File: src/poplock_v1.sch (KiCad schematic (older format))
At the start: 0 parts

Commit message: cicuito mic sem hierarquia
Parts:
- added C1: 10u, symbol C
- added Q?: MMBF170, SOT-23, symbol MMBF170
- added R1: 10000, symbol R
- added U?: MIC_ELECTRET, symbol MIC_ELECTRET
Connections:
- net labels added: +12V, GND, Output
- wire segments 0 -> 9
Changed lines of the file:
@@
 LIBS:valves
 LIBS:L293D
+LIBS:microphone
 LIBS:poplock_v1-cache
 EELAYER 25 0
@@
 F6 "DIRECTION_L" I L 8350 3550 60
 $EndSheet
+$Comp
+L MIC_ELECTRET U?
+U 1 1 57CDCC00
+P 4900 4350
+F 0 "U?" H 4900 4600 60  0000 C CNN
+F 1 "MIC_ELECTRET" H 4900 4000 60  0000 C CNN
+F 2 "" H 4900 4350 60  0000 C CNN
+F 3 "" H 4900 4350 60  0000 C CNN
+	1    4900 4350
+	1    0    0    -1
+$EndComp
+$Comp
+L MMBF170 Q?
+U 1 1 57CDE9F6
+P 5750 4050
+F 0 "Q?" H 5950 4125 50  0000 L CNN
+F 1 "MMBF170" H 5950 4050 50  0000 L CNN
+F 2 "SOT-23" H 5950 3975 50  0000 L CIN
+F 3 "" H 5750 4050 50  0000 L CNN
+	1    5750 4050
+	1    0    0    -1
+$EndComp
+Wire Wire Line
+	5200 4250 5550 4250
+Wire Wire Line
+	5550 4250 5550 4100
+$Comp
+L GND #PWR?
+U 1 1 57CDED40
+P 5950 4750
+F 0 "#PWR?" H 5950 4500 50  0001 C CNN
+F 1 "GND" H 5950 4600 50  0000 C CNN
+F 2 "" H 5950 4750 50  0000 C CNN
+F 3 "" H 5950 4750 50  0000 C CNN
+	1    5950 4750
+	1    0    0    -1
+$EndComp
+Wire Wire Line
+	5950 4450 5950 4750
+Wire Wire Line
+	5200 4450 5950 4450
+Wire Wire Line
+	5850 4250 5850 4450
+$Comp
+L R R1
+U 1 1 57CDF14B
+P 5850 3550
+F 0 "R1" V 5930 3550 50  0000 C CNN
+F 1 "10000" V 5850 3550 50  0000 C CNN
+F 2 "" V 5780 3550 50  0000 C CNN
+F 3 "" H 5850 3550 50  0000 C CNN
+	1    5850 3550
+	1    0    0    -1
+$EndComp
+Wire Wire Line
+	5850 3850 5850 3700
+Wire Wire Line
+	5850 3400 5850 3200
+$Comp
+L +12V #PWR?
+U 1 1 57CDFF14
+P 5850 3200
+F 0 "#PWR?" H 5850 3050 50  0001 C CNN
+F 1 "+12V" H 5850 3340 50  0000 C CNN
+F 2 "" H 5850 3200 50  0000 C CNN
+F 3 "" H 5850 3200 50  0000 C CNN
+	1    5850 3200
+	1    0    0    -1
+$EndComp
+$Comp
+L C C1
+U 1 1 57CE02A0
+P 6200 3800
+F 0 "C1" H 6225 3900 50  0000 L CNN
+F 1 "10u" H 6225 3700 50  0000 L CNN
+F 2 "" H 6238 3650 50  0000 C CNN
+F 3 "" H 6200 3800 50  0000 C CNN
+	1    6200 3800
+	0    1    1    0
+$EndComp
+Wire Wire Line
+	6050 3800 5850 3800
+Connection ~ 5850 3800
+Text GLabel 6550 3800 2    60   Input ~ 0
+Output
+Wire Wire Line
+	6350 3800 6550 3800
 $EndSCHEMATC

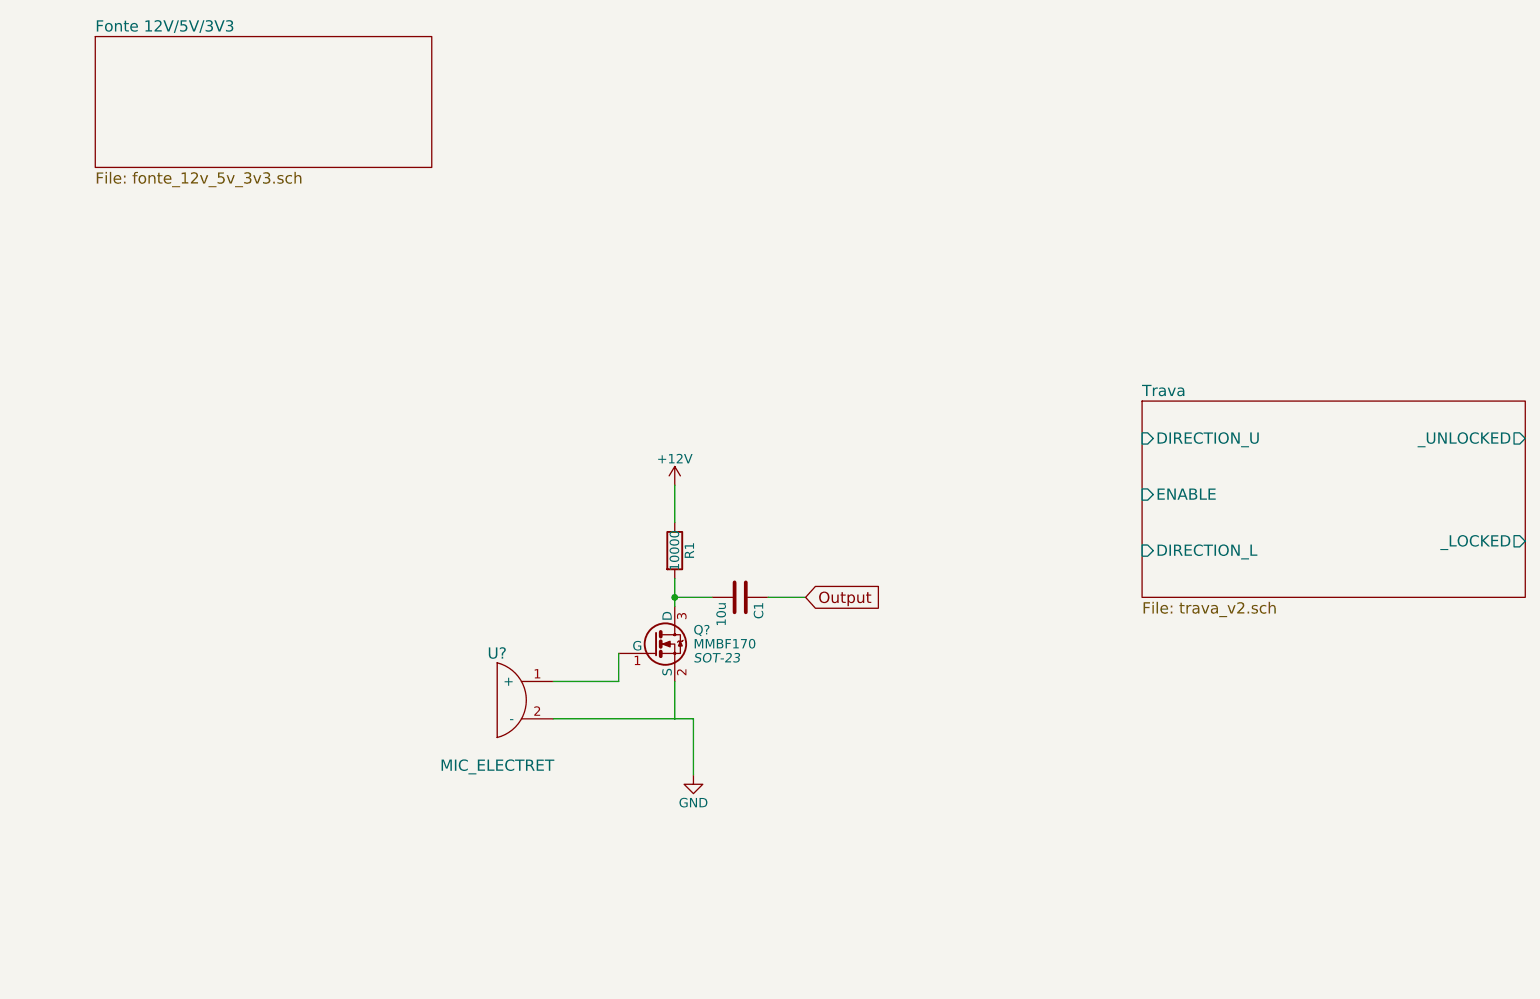
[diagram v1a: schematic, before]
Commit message: Criada hierarquia para o circuito do microfone
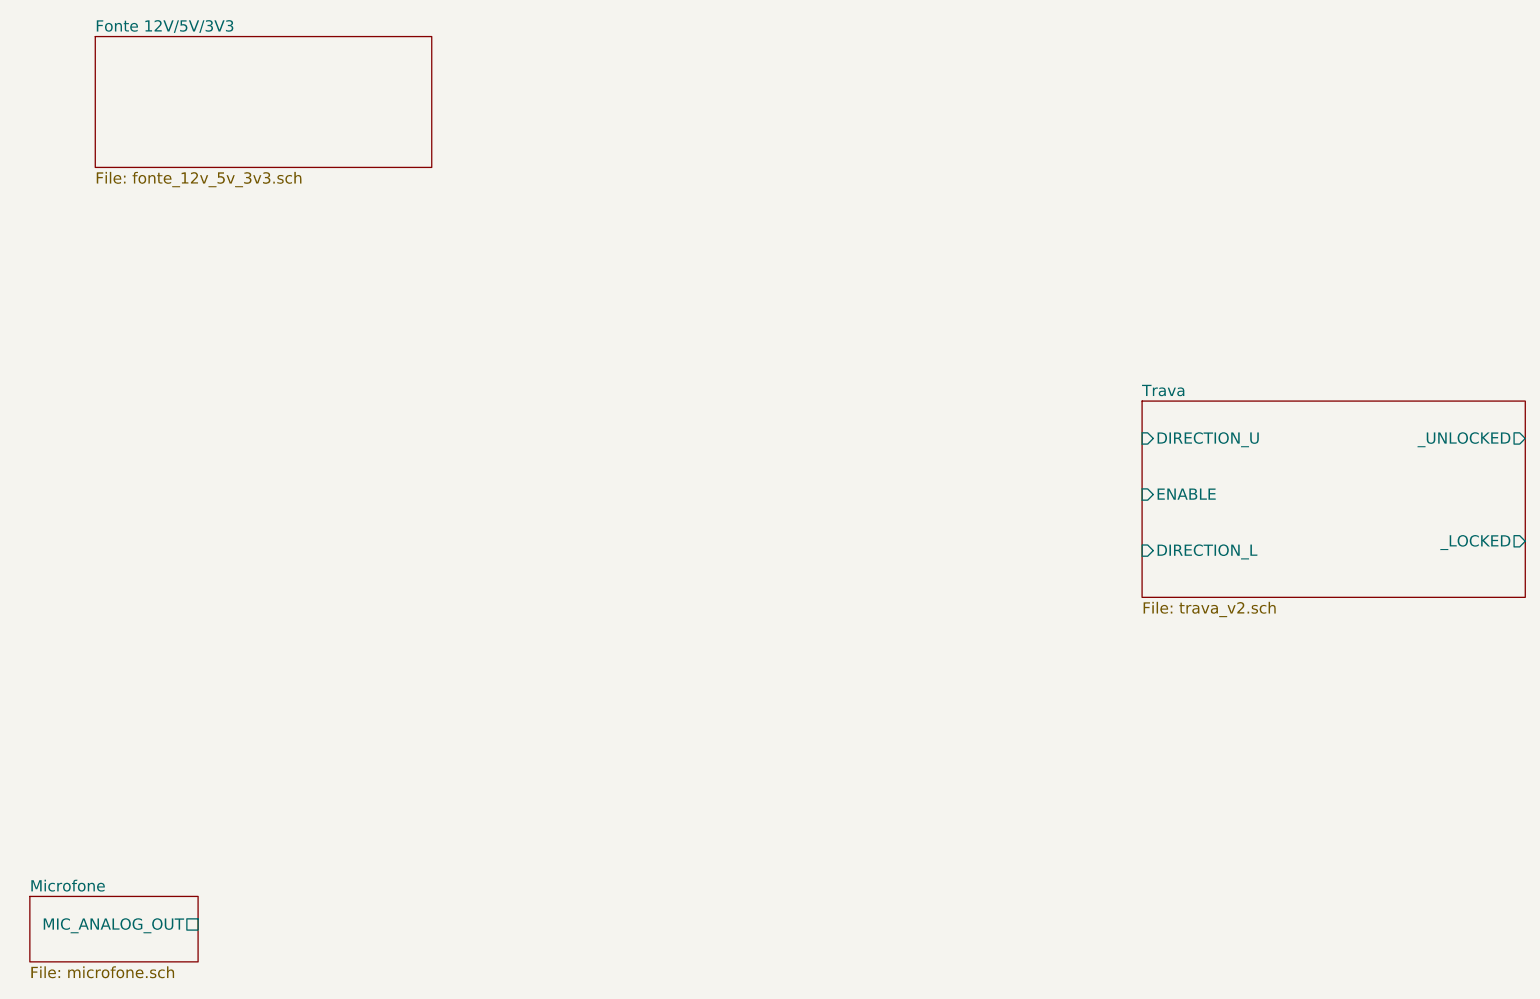
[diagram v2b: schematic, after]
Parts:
- removed C1: 10u, symbol C
- removed Q?: MMBF170, SOT-23, symbol MMBF170
- removed R1: 10000, symbol R
- removed U?: MIC_ELECTRET, symbol MIC_ELECTRET
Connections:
- net labels removed: +12V, GND, Output
- wire segments 9 -> 0
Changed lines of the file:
@@
 LIBS:valves
 LIBS:L293D
-LIBS:microphone
 LIBS:poplock_v1-cache
 EELAYER 25 0
@@
 $Descr A4 11693 8268
 encoding utf-8
-Sheet 1 3
+Sheet 1 4
 Title "Circuito central"
 Date "2016-08-28"
@@
 F6 "DIRECTION_L" I L 8350 3550 60
 $EndSheet
-$Comp
-L MIC_ELECTRET U?
-U 1 1 57CDCC00
-P 4900 4350
-F 0 "U?" H 4900 4600 60  0000 C CNN
-F 1 "MIC_ELECTRET" H 4900 4000 60  0000 C CNN
-F 2 "" H 4900 4350 60  0000 C CNN
-F 3 "" H 4900 4350 60  0000 C CNN
-	1    4900 4350
-	1    0    0    -1
-$EndComp
-$Comp
-L MMBF170 Q?
-U 1 1 57CDE9F6
-P 5750 4050
-F 0 "Q?" H 5950 4125 50  0000 L CNN
-F 1 "MMBF170" H 5950 4050 50  0000 L CNN
-F 2 "SOT-23" H 5950 3975 50  0000 L CIN
-F 3 "" H 5750 4050 50  0000 L CNN
-	1    5750 4050
-	1    0    0    -1
-$EndComp
-Wire Wire Line
-	5200 4250 5550 4250
-Wire Wire Line
-	5550 4250 5550 4100
-$Comp
-L GND #PWR?
-U 1 1 57CDED40
-P 5950 4750
-F 0 "#PWR?" H 5950 4500 50  0001 C CNN
-F 1 "GND" H 5950 4600 50  0000 C CNN
-F 2 "" H 5950 4750 50  0000 C CNN
-F 3 "" H 5950 4750 50  0000 C CNN
-	1    5950 4750
-	1    0    0    -1
-$EndComp
-Wire Wire Line
-	5950 4450 5950 4750
-Wire Wire Line
-	5200 4450 5950 4450
-Wire Wire Line
-	5850 4250 5850 4450
-$Comp
-L R R1
-U 1 1 57CDF14B
-P 5850 3550
-F 0 "R1" V 5930 3550 50  0000 C CNN
-F 1 "10000" V 5850 3550 50  0000 C CNN
-F 2 "" V 5780 3550 50  0000 C CNN
-F 3 "" H 5850 3550 50  0000 C CNN
-	1    5850 3550
-	1    0    0    -1
-$EndComp
-Wire Wire Line
-	5850 3850 5850 3700
-Wire Wire Line
-	5850 3400 5850 3200
-$Comp
-L +12V #PWR?
-U 1 1 57CDFF14
-P 5850 3200
-F 0 "#PWR?" H 5850 3050 50  0001 C CNN
-F 1 "+12V" H 5850 3340 50  0000 C CNN
-F 2 "" H 5850 3200 50  0000 C CNN
-F 3 "" H 5850 3200 50  0000 C CNN
-	1    5850 3200
-	1    0    0    -1
-$EndComp
-$Comp
-L C C1
-U 1 1 57CE02A0
-P 6200 3800
-F 0 "C1" H 6225 3900 50  0000 L CNN
-F 1 "10u" H 6225 3700 50  0000 L CNN
-F 2 "" H 6238 3650 50  0000 C CNN
-F 3 "" H 6200 3800 50  0000 C CNN
-	1    6200 3800
-	0    1    1    0
-$EndComp
-Wire Wire Line
-	6050 3800 5850 3800
-Connection ~ 5850 3800
-Text GLabel 6550 3800 2    60   Input ~ 0
-Output
-Wire Wire Line
-	6350 3800 6550 3800
+$Sheet
+S 2400 5400 900  350
+U 57CE139B
+F0 "Microfone" 60
+F1 "microfone.sch" 60
+F2 "MIC_ANALOG_OUT" U R 3300 5550 60
+$EndSheet
 $EndSCHEMATC
